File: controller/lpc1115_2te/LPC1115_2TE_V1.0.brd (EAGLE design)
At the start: 30.5 x 58.1 mm, 52 parts, among them IC1 LPC1115, IC2 BD9G101, Q1 BC856, Q2 BC847C, Q3 BCP52, Q4 FA-

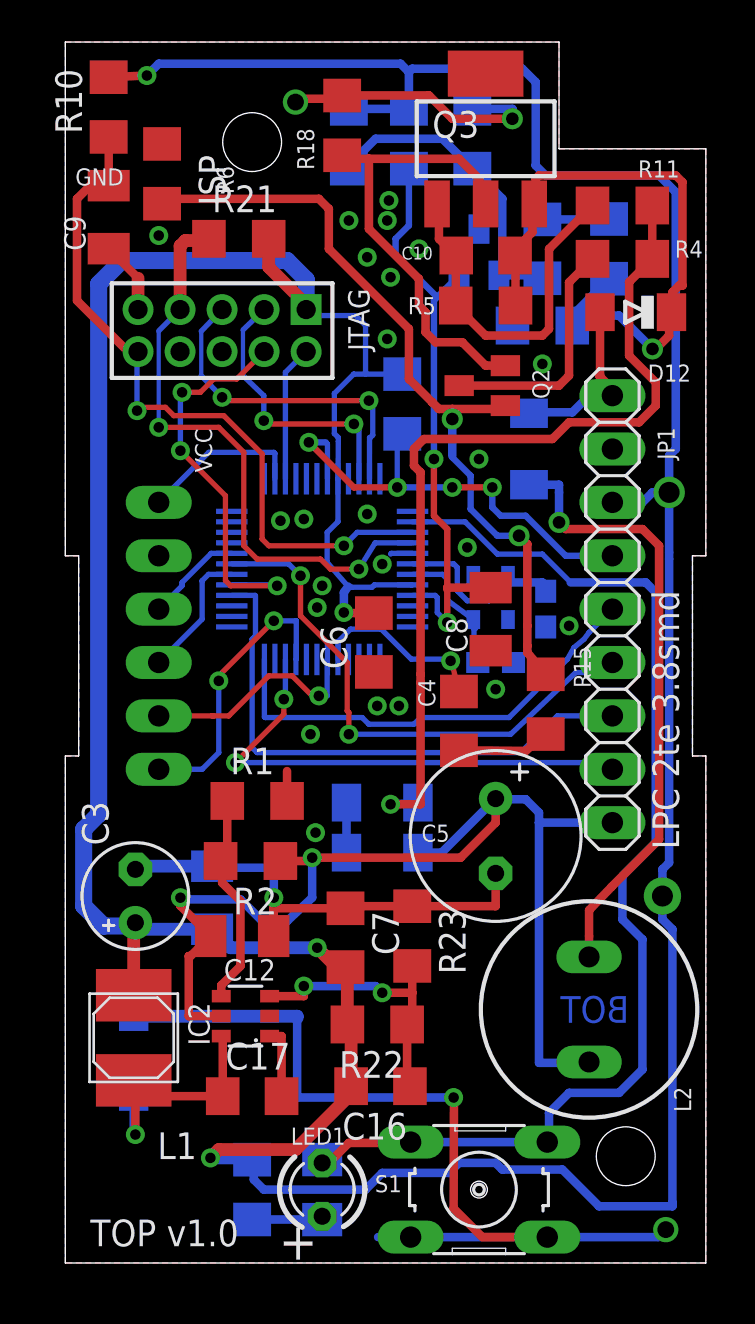
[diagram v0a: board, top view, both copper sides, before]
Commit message: BUS-ADC zugefügt
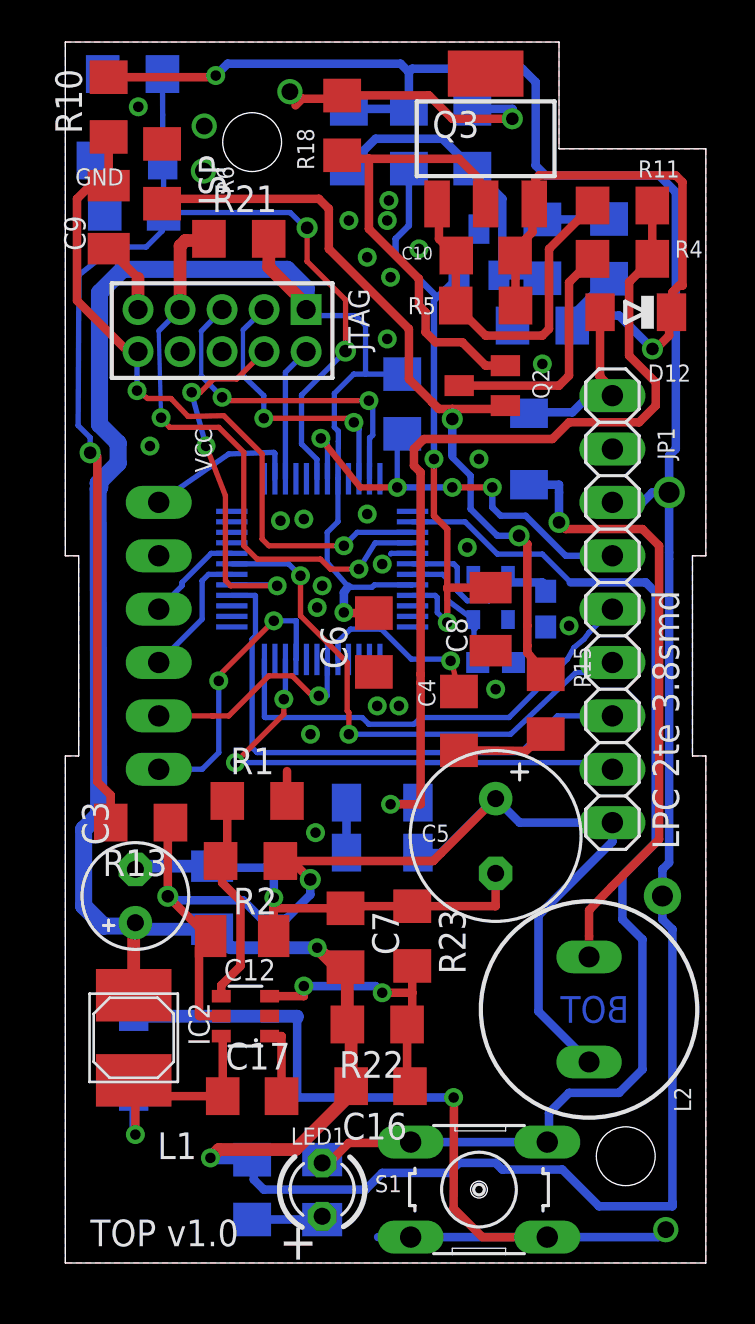
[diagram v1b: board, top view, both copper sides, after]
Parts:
- added C20: (no value), rcl:C1206
- added D1: 3V6, diode:MINIMELF
- added R13: 91k, rcl:R1206
- added R16: 10k, rcl:R1206
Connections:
- net BUS_V: now also C20.2, D1.C, R13.2, R16.1
- net EIB_DC: now also R13.1
- net GND: now also C20.1, D1.A, R16.2
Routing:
- net BUS_V: track 0.00 -> 60.1 mm, vias 0 -> 3
- net EIB_DC: track 54.5 -> 57.9 mm
- net SWCLK: track 19.3 -> 18.2 mm
- net PWM: track 22.5 -> 21.7 mm
- net RESET: track 34.2 -> 33.5 mm
- net GND: vias 28 -> 31
